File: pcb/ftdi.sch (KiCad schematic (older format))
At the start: 42 parts, among them U2 FT2232HL, U3 M93C46-WMN6TP, U4 MC74VHC1GT04DFT1, U5 74AHC125BQ,115, Y1 ECS-120-18-33-JEM-TR

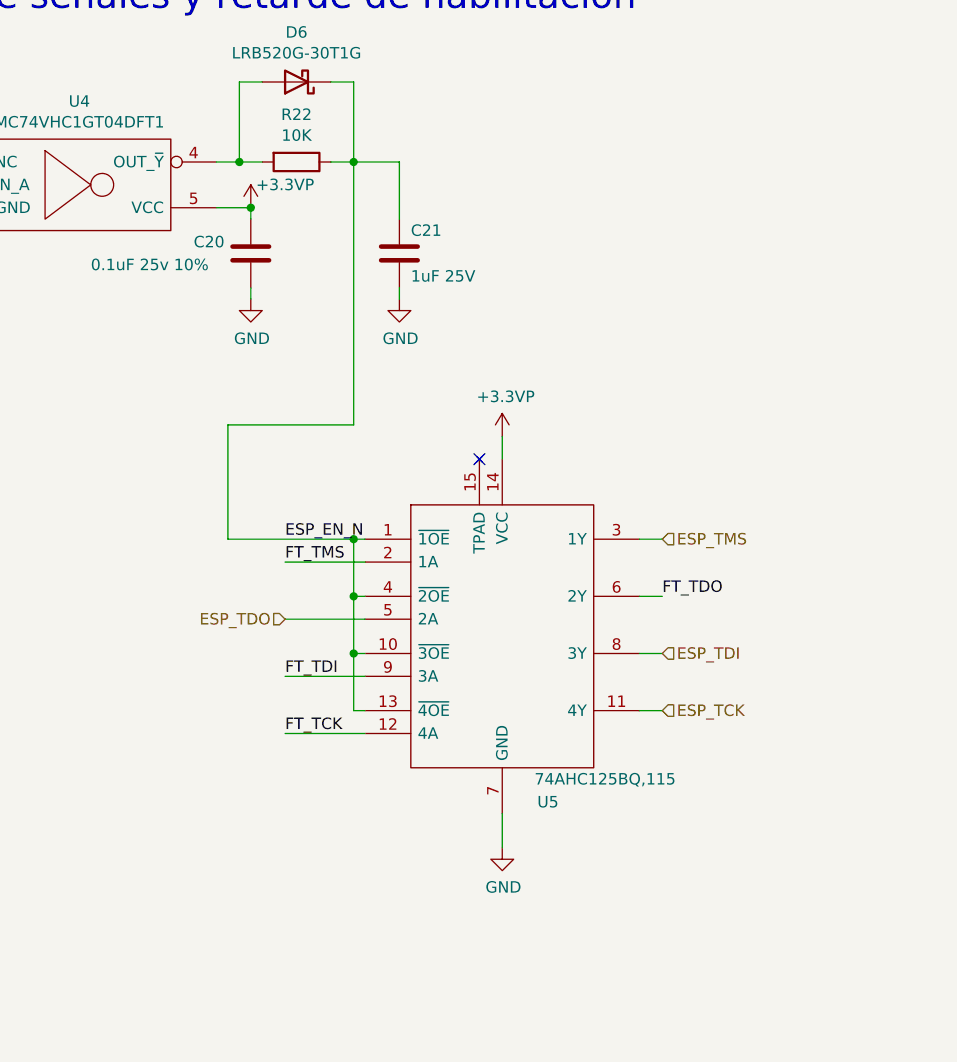
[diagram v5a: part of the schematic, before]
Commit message: Primer versión ruteo terminada
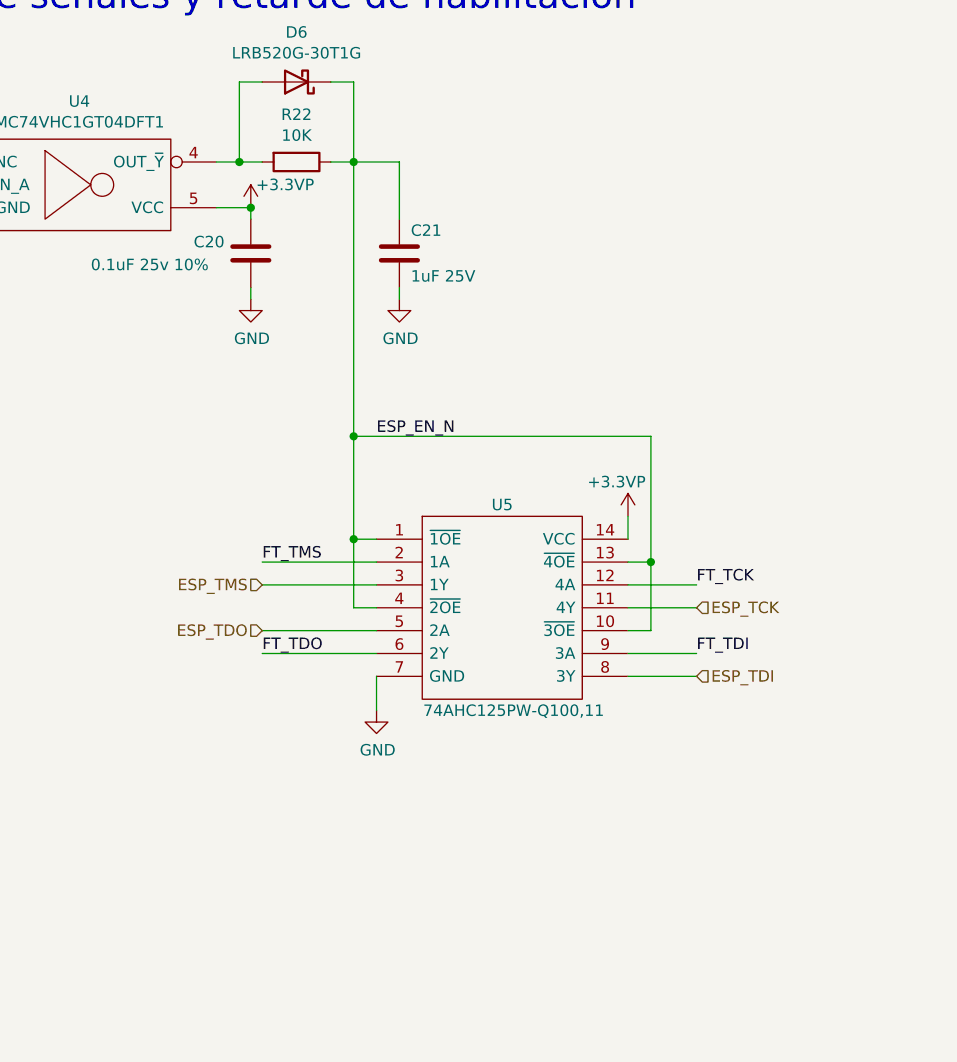
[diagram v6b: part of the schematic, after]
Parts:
- removed U5: 74AHC125BQ,115, SamacSys_Parts:QFN50P250X300X100-15N-D, symbol SamacSys_Parts:74AHC125BQ,115
- added U5: 74AHC125PW-Q100,11, SamacSys_Parts:SOP65P640X110-14N, symbol SamacSys_Parts:74AHC125PW-Q100,11
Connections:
- net +3.3VP: now also U5.14 (VCC)
- net ESP_EN_N: now also U5.1 (~1OE), U5.10 (~3OE), U5.13 (~4OE), U5.4 (~2OE)
- net ESP_TCK: now also U5.11 (4Y)
- net ESP_TDI: now also U5.8 (3Y)
- net ESP_TDO: now also U5.5 (2A)
- net ESP_TMS: now also U5.3 (1Y)
- net FT_TCK: now also U5.12 (4A)
- net FT_TDI: now also U5.9 (3A)
- net FT_TDO: now also U5.6 (2Y)
- net FT_TMS: now also U5.2 (1A)
- net GND: now also U5.7 (GND)
- no-connect marks 26 -> 25
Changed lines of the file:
@@
 EEDATA
-$Comp
-L SamacSys_Parts:74AHC125BQ,115 U5
-U 1 1 60ED1A1F
-P 9250 5200
-F 0 "U5" H 10050 4300 50  0000 C CNN
-F 1 "74AHC125BQ,115" H 10300 4400 50  0000 C CNN
-F 2 "SamacSys_Parts:QFN50P250X300X100-15N-D" H 10300 5600 50  0001 L CNN
-F 3 "https://assets.nexperia.com/documents/data-sheet/74AHC_AHCT125.pdf" H 10300 5500 50  0001 L CNN
-F 4 "74AHC(T)125 - Quad buffer/line driver; 3-state@en-us" H 10300 5400 50  0001 L CNN "Description"
-F 5 "1" H 10300 5300 50  0001 L CNN "Height"
-F 6 "771-74AHC125BQ-G" H 10300 5200 50  0001 L CNN "Mouser Part Number"
-F 7 "https://www.mouser.co.uk/ProductDetail/Nexperia/74AHC125BQ115?qs=P62ublwmbi8QjemqxPiMnQ%3D%3D" H 10300 5100 50  0001 L CNN "Mouser Price/Stock"
-F 8 "Nexperia" H 10300 5000 50  0001 L CNN "Manufacturer_Name"
-F 9 "74AHC125BQ,115" H 10300 4900 50  0001 L CNN "Manufacturer_Part_Number"
-	1    9250 5200
-	1    0    0    -1
-$EndComp
 $Comp
 L power:GND #PWR023
 U 1 1 60ED3C1C
-P 9850 6300
-F 0 "#PWR023" H 9850 6050 50  0001 C CNN
-F 1 "GND" H 9855 6127 50  0000 C CNN
-F 2 "" H 9850 6300 50  0001 C CNN
-F 3 "" H 9850 6300 50  0001 C CNN
-	1    9850 6300
-	1    0    0    -1
-$EndComp
-Wire Wire Line
-	9850 6300 9850 6150
-Wire Wire Line
-	9850 4600 9850 4500
-NoConn ~ 9750 4600
-Wire Wire Line
-	10450 4950 10550 4950
-Wire Wire Line
-	10450 5200 10550 5200
-Wire Wire Line
-	10450 5450 10550 5450
-Wire Wire Line
-	10450 5700 10550 5700
-Wire Wire Line
-	9250 4950 9200 4950
-Wire Wire Line
-	9250 5050 8900 5050
-Wire Wire Line
-	9250 5200 9200 5200
-Wire Wire Line
-	9250 5300 8900 5300
-Wire Wire Line
-	9250 5450 9200 5450
-Wire Wire Line
-	9250 5550 8900 5550
-Wire Wire Line
-	9250 5700 9200 5700
-Wire Wire Line
-	9250 5800 8900 5800
-Wire Wire Line
-	9200 4950 9200 5200
-Connection ~ 9200 5200
-Wire Wire Line
-	9200 5200 9200 5450
-Connection ~ 9200 5450
-Wire Wire Line
-	9200 5450 9200 5700
-Connection ~ 9200 4950
-Text Label 8900 4950 0    50   ~ 0
+P 9300 5700
+F 0 "#PWR023" H 9300 5450 50  0001 C CNN
+F 1 "GND" H 9305 5527 50  0000 C CNN
+F 2 "" H 9300 5700 50  0001 C CNN
+F 3 "" H 9300 5700 50  0001 C CNN
+	1    9300 5700
+	1    0    0    -1
+$EndComp
+Wire Wire Line
+	9300 5700 9300 5550
+Text Label 9300 4500 0    50   ~ 0
 ESP_EN_N
-Text Label 8900 5050 0    50   ~ 0
+Text Label 8800 5050 0    50   ~ 0
 FT_TMS
-Text Label 10550 5200 0    50   ~ 0
+Text Label 8800 5450 0    50   ~ 0
 FT_TDO
-Text Label 8900 5550 0    50   ~ 0
+Text Label 10700 5450 0    50   ~ 0
 FT_TDI
-Text Label 8900 5800 0    50   ~ 0
+Text Label 10700 5150 0    50   ~ 0
 FT_TCK
 $Comp
@@
 L power:+3.3VP #PWR022
 U 1 1 60F0D884
-P 9850 4500
-F 0 "#PWR022" H 10000 4450 50  0001 C CNN
-F 1 "+3.3VP" H 9865 4673 50  0000 C CNN
-F 2 "" H 9850 4500 50  0001 C CNN
-F 3 "" H 9850 4500 50  0001 C CNN
-	1    9850 4500
-	1    0    0    -1
-$EndComp
-$Comp
-L power:+3.3VP #PWR026
-U 1 1 60F0E085
-P 8750 3500
-F 0 "#PWR026" H 8900 3450 50  0001 C CNN
-F 1 "+3.3VP" H 8900 3600 50  0000 C CNN
-F 2 "" H 8750 3500 50  0001 C CNN
-F 3 "" H 8750 3500 50  0001 C CNN
-	1    8750 3500
+P 10400 4850
+F 0 "#PWR022" H 10550 4800 50  0001 C CNN
+F 1 "+3.3VP" H 10350 5000 50  0000 C CNN
+F 2 "" H 10400 4850 50  0001 C CNN
+F 3 "" H 10400 4850 50  0001 C CNN
+	1    10400 4850
 	1    0    0    -1
 $EndComp
@@
 	1    0    0    -1
 $EndComp
-Wire Wire Line
-	8600 3500 8750 3500
-Wire Wire Line
-	8750 3500 8750 3550
-Connection ~ 8750 3500
 Wire Wire Line
 	8750 3850 8750 3900
@@
 Text HLabel 6150 5000 2    50   Output ~ 0
 FT_nDTR
-Text HLabel 8900 5300 0    50   Input ~ 0
+Text HLabel 8800 5350 0    50   Input ~ 0
 ESP_TDO
-Text HLabel 10550 4950 2    50   Input ~ 0
+Text HLabel 8800 5150 0    50   Input ~ 0
 ESP_TMS
-Text HLabel 10550 5450 2    50   Input ~ 0
-ESP_TDI
-Text HLabel 10550 5700 2    50   Input ~ 0
+Text HLabel 10700 5250 2    50   Input ~ 0
 ESP_TCK
 Wire Notes Line
@@
 Buffers de señales y retarde de habilitación
 Wire Wire Line
-	9200 3300 9200 4450
-Wire Wire Line
-	9200 4450 8650 4450
-Wire Wire Line
-	8650 4450 8650 4950
-Wire Wire Line
-	8650 4950 9200 4950
-Wire Wire Line
 	4850 1800 4850 1650
 $Comp
@@
 Wire Wire Line
 	4250 2500 4250 2400
+$Comp
+L SamacSys_Parts:74AHC125PW-Q100,11 U5
+U 1 1 6121C450
+P 9300 4950
+F 0 "U5" H 9850 5100 50  0000 C CNN
+F 1 "74AHC125PW-Q100,11" H 9900 4200 50  0000 C CNN
+F 2 "SamacSys_Parts:SOP65P640X110-14N" H 10250 5050 50  0001 L CNN
+F 3 "https://assets.nexperia.com/documents/data-sheet/74AHC_AHCT125_Q100.pdf" H 10250 4950 50  0001 L CNN
+F 4 "74AHC(T)125-Q100 - Quad buffer/line driver; 3-state@en-us" H 10250 4850 50  0001 L CNN "Description"
+F 5 "1.1" H 10250 4750 50  0001 L CNN "Height"
+F 6 "771-74AHC125PWQ10011" H 10250 4650 50  0001 L CNN "Mouser Part Number"
+F 7 "https://www.mouser.co.uk/ProductDetail/Nexperia/74AHC125PW-Q10011?qs=vnbNJPHmPnMSFphxgi1ssg%3D%3D" H 10250 4550 50  0001 L CNN "Mouser Price/Stock"
+F 8 "Nexperia" H 10250 4450 50  0001 L CNN "Manufacturer_Name"
+F 9 "74AHC125PW-Q100,11" H 10250 4350 50  0001 L CNN "Manufacturer_Part_Number"
+	1    9300 4950
+	1    0    0    -1
+$EndComp
+Wire Wire Line
+	9300 5250 9200 5250
+Wire Wire Line
+	9200 5250 9200 4950
+Wire Wire Line
+	9200 4950 9300 4950
+Wire Wire Line
+	10400 5350 10500 5350
+Wire Wire Line
+	10500 5350 10500 5050
+Wire Wire Line
+	10500 5050 10400 5050
+Wire Wire Line
+	10500 5050 10500 4500
+Connection ~ 10500 5050
+Wire Wire Line
+	9200 3300 9200 4500
+Wire Wire Line
+	9300 5050 8800 5050
+Wire Wire Line
+	9300 5150 8800 5150
+Wire Wire Line
+	9300 5350 8800 5350
+Wire Wire Line
+	9300 5450 8800 5450
+Wire Wire Line
+	10400 5150 10700 5150
+Wire Wire Line
+	10400 5250 10700 5250
+Wire Wire Line
+	10400 5450 10700 5450
+Wire Wire Line
+	10400 5550 10700 5550
+Text HLabel 10700 5550 2    50   Input ~ 0
+ESP_TDI
+Wire Wire Line
+	9200 4500 10500 4500
+Wire Wire Line
+	9200 4950 9200 4500
+Connection ~ 9200 4950
+Connection ~ 9200 4500
+Wire Wire Line
+	10400 4950 10400 4850
+$Comp
+L power:+3.3VP #PWR026
+U 1 1 60F0E085
+P 8750 3500
+F 0 "#PWR026" H 8900 3450 50  0001 C CNN
+F 1 "+3.3VP" H 8900 3600 50  0000 C CNN
+F 2 "" H 8750 3500 50  0001 C CNN
+F 3 "" H 8750 3500 50  0001 C CNN
+	1    8750 3500
+	1    0    0    -1
+$EndComp
+Wire Wire Line
+	8600 3500 8750 3500
+Wire Wire Line
+	8750 3500 8750 3550
+Connection ~ 8750 3500
 $EndSCHEMATC
